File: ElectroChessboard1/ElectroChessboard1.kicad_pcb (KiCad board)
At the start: 4 copper layers, 306.2 x 314.8 mm, 243 parts, among them IC1 A3213ELHLT-T, IC10 A3213ELHLT-T, IC11 A3213ELHLT-T, IC12 A3213ELHLT-T, IC13 A3213ELHLT-T, IC14 A3213ELHLT-T, IC15 A3213ELHLT-T, IC16 A3213ELHLT-T, IC17 A3213ELHLT-T, IC18 ADG708BRUZ-REEL7, IC19 A3213ELHLT-T, IC2 A3213ELHLT-T, IC20 A3213ELHLT-T, IC21 A3213ELHLT-T, IC22 A3213ELHLT-T, IC23 A3213ELHLT-T, IC24 A3213ELHLT-T, IC25 A3213ELHLT-T, IC26 A3213ELHLT-T, IC27 A3213ELHLT-T, IC28 A3213ELHLT-T, IC29 A3213ELHLT-T, IC3 A3213ELHLT-T, IC30 A3213ELHLT-T, IC31 A3213ELHLT-T, IC32 A3213ELHLT-T, IC33 A3213ELHLT-T, IC34 A3213ELHLT-T, IC35 ADG708BRUZ-REEL7, IC36 ADG708BRUZ-REEL7, IC37 A3213ELHLT-T, IC38 A3213ELHLT-T, IC39 A3213ELHLT-T, IC4 A3213ELHLT-T, IC40 A3213ELHLT-T, IC41 A3213ELHLT-T, IC42 A3213ELHLT-T, IC43 A3213ELHLT-T, IC44 A3213ELHLT-T, IC45 A3213ELHLT-T, IC46 A3213ELHLT-T, IC47 A3213ELHLT-T, IC48 A3213ELHLT-T, IC49 A3213ELHLT-T, IC5 A3213ELHLT-T, IC50 A3213ELHLT-T, IC51 A3213ELHLT-T, IC52 A3213ELHLT-T, IC53 ADG708BRUZ-REEL7, IC54 ADG708BRUZ-REEL7, IC55 A3213ELHLT-T, IC56 A3213ELHLT-T, IC57 A3213ELHLT-T, IC58 A3213ELHLT-T, IC59 A3213ELHLT-T, IC6 A3213ELHLT-T, IC60 A3213ELHLT-T, IC61 A3213ELHLT-T, IC62 A3213ELHLT-T, IC63 A3213ELHLT-T, IC64 A3213ELHLT-T, IC65 A3213ELHLT-T, IC66 A3213ELHLT-T, IC67 A3213ELHLT-T, IC68 A3213ELHLT-T, IC69 A3213ELHLT-T, IC7 A3213ELHLT-T, IC70 A3213ELHLT-T, IC71 ADG708BRUZ-REEL7, IC72 ADG708BRUZ-REEL7, IC73 CD74HC154M96, IC74 CD74HC154M96, IC75 DS1307Z+T&R, IC76 CD74HC154M96, IC77 CD74HC154M96, IC8 A3213ELHLT-T, IC9 ADG708BRUZ-REEL7, J2 TYPE-C-31-M-12, J3 Conn_01x04_Pin, J5 Conn_01x06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

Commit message: update
.
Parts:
- moved J6 225.5 mm to (264.4, 319.5), turned to 180 degrees
- moved R1 44.6 mm to (289.8, 318.0), turned to 90 degrees
- moved D3 42.5 mm to (288.0, 314.0)
- moved R39 28.3 mm to (306.2, 325.2), turned to -90 degrees
- moved R38 2.32 mm to (310.0, 317.8)
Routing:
- net SafeVCC: track 1372.4 -> 1586.0 mm, vias 9 -> 13
- net LED_A0_1: track 187.2 -> 71.7 mm
- net FT232RLreset: track 76.3 -> 108.2 mm, vias 2 -> 3
- net SafeGND: track 3250.1 -> 3271.2 mm
- net PB2: track 182.7 -> 202.9 mm, vias 3 -> 4
- net PB1: track 184.0 -> 201.4 mm, vias 2 -> 3
- net PB3: track 181.8 -> 191.5 mm
- net Net-(IC75-SDA): track 17.1 -> 21.8 mm, vias 2 -> 3
- net Net-(IC75-SCL): track 18.3 -> 22.2 mm

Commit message: update
.
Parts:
- moved S1 16.1 mm to (304.1, 108.8), turned to 90 degrees
- moved S2 15.9 mm to (304.1, 124.8), turned to 90 degrees
- turned S3 to 90 degrees
- turned S4 to 90 degrees
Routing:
- net SafeGND: track 3271.2 -> 3600.0 mm, vias 8 -> 10
- net A2_0: track 0.00 -> 284.0 mm, vias 0 -> 2
- net SafeVCC: track 1586.0 -> 1866.0 mm, vias 13 -> 29
- net EN_0: track 0.00 -> 270.1 mm, vias 0 -> 4
- net A2_2: track 0.00 -> 269.2 mm, vias 0 -> 3
- net A1_0: track 0.00 -> 268.9 mm, vias 0 -> 2
- net A2_1: track 0.00 -> 268.8 mm, vias 0 -> 3
- net A1_2: track 0.00 -> 267.6 mm, vias 0 -> 3
- net A1_1: track 0.00 -> 264.0 mm, vias 0 -> 3
- net EN_2: track 0.00 -> 262.6 mm, vias 0 -> 3
- net A0_0: track 0.00 -> 258.1 mm, vias 0 -> 2
- net EN_1: track 0.00 -> 254.6 mm, vias 0 -> 3
- net A0_1: track 0.00 -> 254.6 mm, vias 0 -> 4
- net A0_2: track 0.00 -> 250.8 mm, vias 0 -> 3
- net A1_3: track 0.00 -> 230.0 mm, vias 0 -> 3
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
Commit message: Major wiring done, only VCCs and GNDs left
Major wiring done, only VCCs and GNDs left
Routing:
- net HallOUT1: track 4.54 -> 224.4 mm, vias 1 -> 5
- net LED_A2_1: track 2.79 -> 219.7 mm, vias 1 -> 4
- net LED_A3_1: track 2.44 -> 214.3 mm, vias 1 -> 4
- net Net-(IC75-SCL): track 22.2 -> 229.5 mm, vias 2 -> 3
- net Net-(IC75-SDA): track 21.8 -> 222.5 mm, vias 3 -> 5
- net HallOUT2: track 1.94 -> 198.9 mm, vias 1 -> 5
- net HallOUT3: track 0.00 -> 180.2 mm, vias 0 -> 4
- net HallOUT4: track 2.94 -> 139.2 mm, vias 1 -> 3
- net HallOUT5: track 4.94 -> 109.7 mm, vias 1 -> 2
- net HallOUT6: track 5.19 -> 76.0 mm, vias 1 -> 2

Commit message: update
27 wiring connections left to make
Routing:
- net SafeVCC: track 1866.0 -> 4481.6 mm, vias 29 -> 98
- net HallOUT0: track 4.94 -> 261.1 mm, vias 1 -> 5
- net LED_A0_2: track 0.00 -> 180.9 mm, vias 0 -> 3
- net A1_3: track 230.0 -> 230.7 mm

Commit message: Wiring done
TODO: move silkscreen layers to safety, add power status LED
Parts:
- moved C7 23.9 mm to (159.2, 278.0), turned to 180 degrees
- moved R55 18.1 mm to (253.0, 285.8), turned to 180 degrees
- moved R3 17.4 mm to (162.0, 286.5), turned to 180 degrees
- moved R36 14.8 mm to (188.8, 284.0), turned to 180 degrees
- moved C12 9.45 mm to (251.2, 293.5)
- moved R2 7.70 mm to (118.0, 294.5), turned to 180 degrees
- moved C6 4.37 mm to (111.5, 294.5)
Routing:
- net SafeGND: track 3600.0 -> 3918.9 mm, vias 10 -> 15
- net SafeVCC: track 4481.6 -> 4632.6 mm, vias 98 -> 107
- net FT232RLtx: track 96.4 -> 204.6 mm, vias 2 -> 6
- net LED_EN_0: track 207.2 -> 219.8 mm
- net LED_EN_1: track 147.6 -> 154.5 mm
- net LED_EN_3: track 67.2 -> 73.6 mm
- net Net-(D21-A): track 0.00 -> 2.75 mm
- net LED_EN_2: track 129.9 -> 131.7 mm
- net Net-(IC70-VOUT): track 47.5 -> 48.9 mm

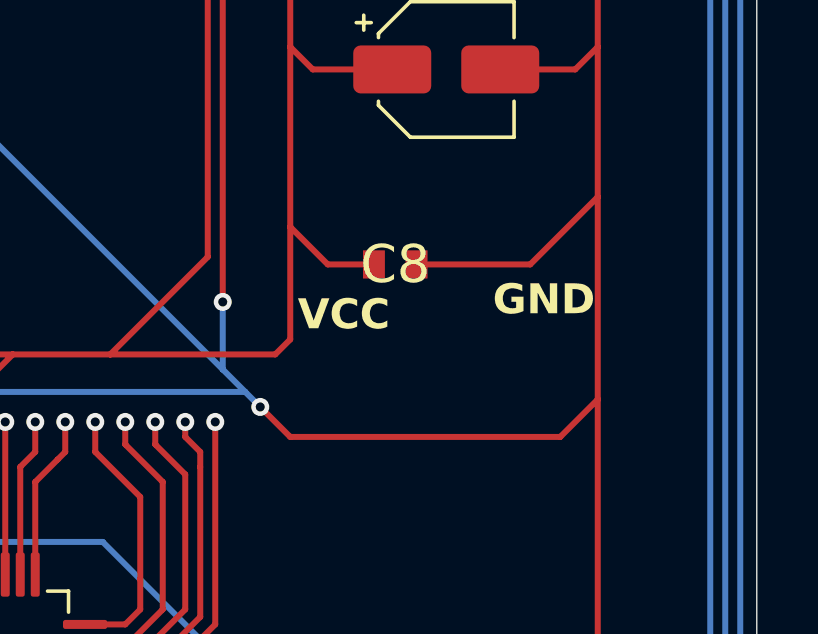
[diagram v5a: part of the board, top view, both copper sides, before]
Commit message: Added power status LED
TODO: Move silkscreen texts out of soldiermasks
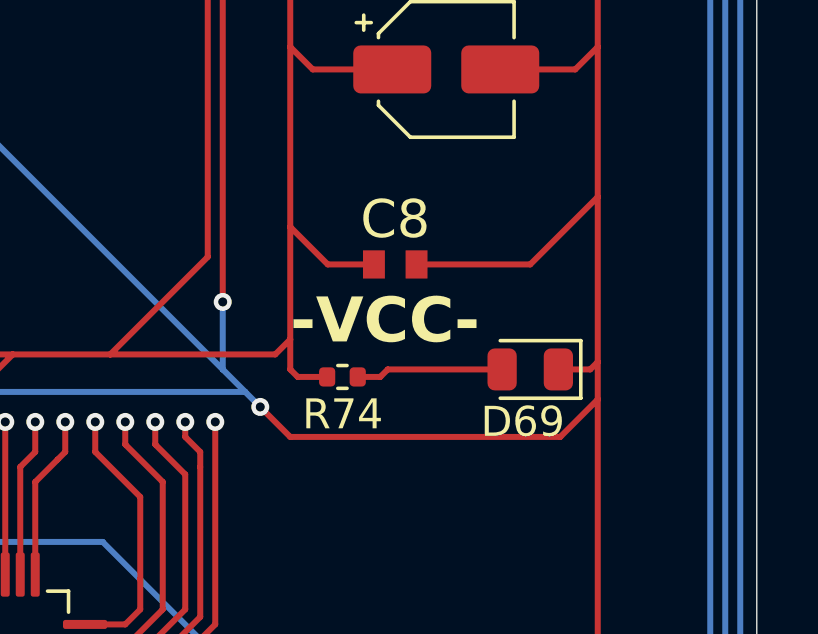
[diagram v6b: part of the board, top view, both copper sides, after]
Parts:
- added D69: LED, LED_SMD:LED_0805_2012Metric, F.Cu at (318.0, 288.5)
- added R74: R, Resistor_SMD:R_0402_1005Metric, F.Cu at (311.7, 288.8)
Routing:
- net Net-(D69-A): track 0.00 -> 4.92 mm
- net SafeVCC: track 4632.6 -> 4634.9 mm
- net SafeGND: track 3918.9 -> 3920.3 mm
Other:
- board text added: "-VCC-"
- board text removed: "GND"
- board text removed: "VCC"
